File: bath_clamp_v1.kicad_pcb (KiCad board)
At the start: 6 copper layers, 83.8 x 48.3 mm, 163 parts, among them IC1 DAC53401DSGR, J1 105-1103-001, J2 105-1103-001, J3 105-1103-001, J4 HDMI_A, K1 1462042-8, K2 1462042-8, Q1 MBT3904DW1T1G, Q2 BC856, Q3 MBT3904DW1T1G, Q4 MBT3904DW1T1G, U1 OPA828, U10 LP2951-3.3_SOIC, U11 OPA991S, U12 TCA9555DBR, U13 TCA9555DBR, U14 DG412xUE, U15 OPA828, U16 TMUX6111PWR, U17 DG412xUE, U18 AD8421ARZ, U19 TMUX6136PWR, U2 ADG1208, U20 TMUX6111PWR, U21 TMUX6111PWR, U22 TMUX6136PWR, U23 OPA188xxDBV, U24 LMP8350MA_NOPB, U25 OPA2156xD, U3 G6L-1F-TR-DC5, U4 G6L-1F-TR-DC5, U5 G6L-1F-TR-DC5, U6 24AA025UID, U7 LM337L_SO8, U8 OPA2156xD, U9 MCP1804x-3302xOT

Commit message: freerouter updates; close to submission
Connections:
- U20 pad 10: /bath_clamp_v1_1/AMP_OUT -> /bath_clamp_v1_1/INAMP_OUT

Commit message: before autoroute
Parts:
- moved H7 50.1 mm to (4.00, -44.0)
- moved C17 50.0 mm to (13.6, -40.1)
- moved C33 50.0 mm to (37.1, -37.8)
- moved C34 50.0 mm to (31.3, -37.2)
- moved C35 50.0 mm to (34.3, -37.2)
- moved C40 50.0 mm to (77.4, -9.89)
- moved C41 50.0 mm to (44.9, -18.0)
- moved D1 50.0 mm to (70.2, -11.0)
- moved D4 50.0 mm to (68.5, -4.31)
- moved J1 50.0 mm to (79.8, -26.6)
- moved K1 50.0 mm to (70.4, -15.0)
- moved K2 50.0 mm to (70.4, -26.4)
- moved Q3 50.0 mm to (68.8, -7.23)
- moved R11 50.0 mm to (70.0, -7.61)
- moved R12 50.0 mm to (71.7, -7.61)
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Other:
- net class Default: clearance 0.1524 -> 0.127; trace_width 0.1524 -> 0.127; via_dia 0.7 -> 0.6
- rule trace_clearance: 0.1524 -> 0.127

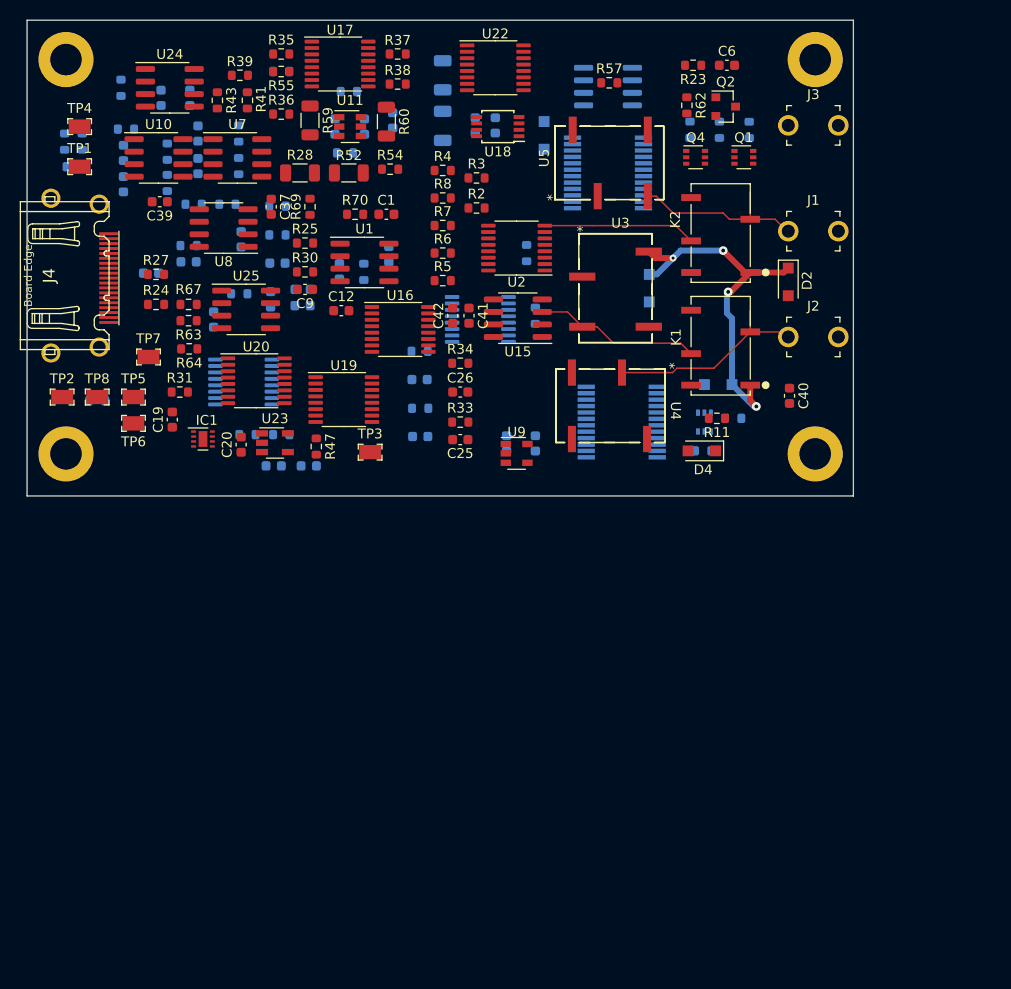
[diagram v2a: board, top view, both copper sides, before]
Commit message: clamp files at submission to JLCPCB
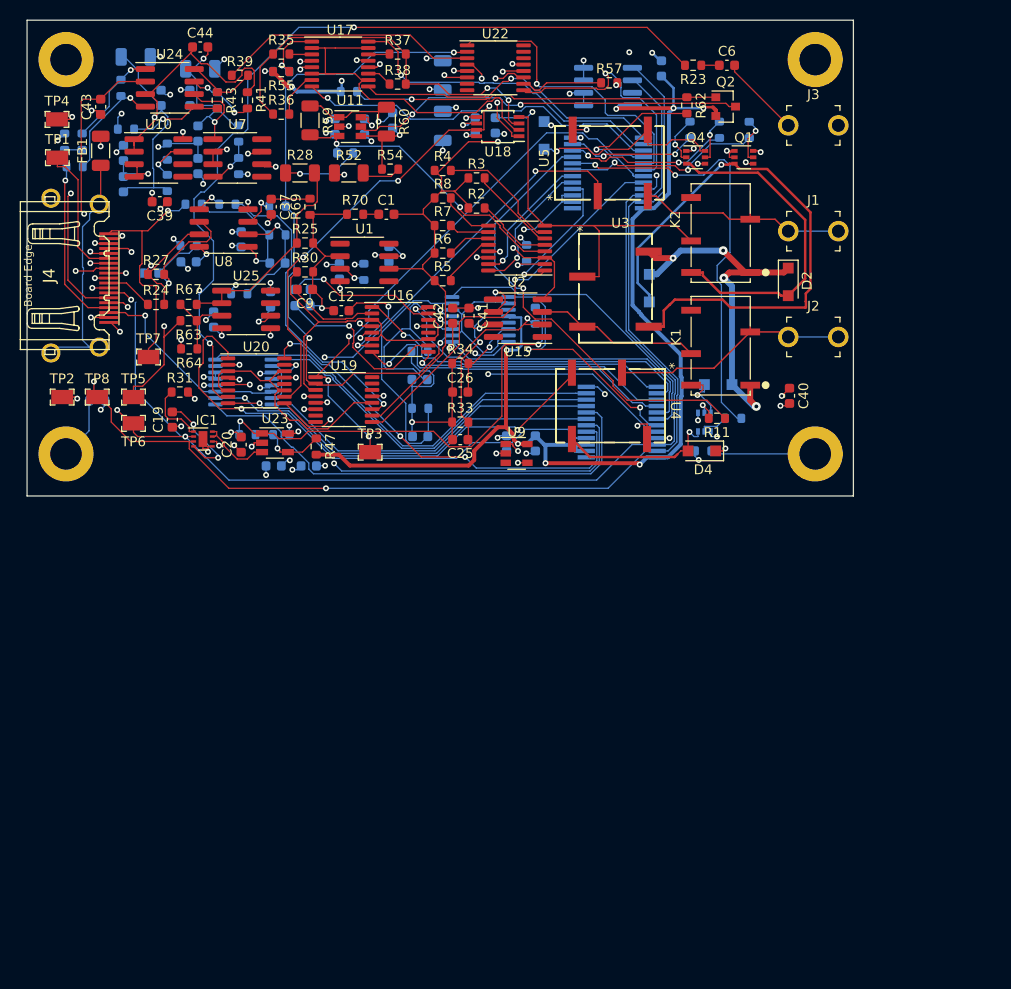
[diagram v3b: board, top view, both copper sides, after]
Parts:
- added C43: 0.1u, Capacitor_SMD:C_0603_1608Metric, F.Cu at (7.52, -39.2)
- added C44: 0.1u, Capacitor_SMD:C_0603_1608Metric, F.Cu at (17.6, -45.3)
- added C45: 10u, Capacitor_SMD:C_1206_3216Metric, B.Cu at (11.1, -44.3)
- added C46: 10u, Capacitor_SMD:C_1206_3216Metric, B.Cu at (17.6, -43.1)
- added C47: 0.1u, Capacitor_SMD:C_0603_1608Metric, B.Cu at (64.4, -43.1)
- added FB1: Ferrite_Bead, Capacitor_SMD:C_1206_3216Metric, F.Cu at (7.52, -34.7)
- added R65: DNI, Resistor_SMD:R_0603_1608Metric, B.Cu at (19.4, -39.9)
- C17, C18: value 0.1u -> 0.01u
- R41: value 1k -> 10k
- moved TP1 2.44 mm to (3.12, -34.0)
- moved TP4 2.41 mm to (3.09, -37.9)
- moved H5 1.22 mm to (4.00, -4.00)
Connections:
- J4 pad SH: GND -> Net-(FB1-Pad1)
- R41 pad 1: +7V -> /bath_clamp_v1_1/adc_driver/LMP_EN
- R41 pad 2: Net-(R41-Pad2) -> +7V
- U24 pad 7: Net-(R41-Pad2) -> /bath_clamp_v1_1/adc_driver/LMP_EN
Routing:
- net +3V3: track 0.00 -> 167.3 mm, vias 0 -> 10
- net /SCL: track 0.00 -> 140.8 mm, vias 0 -> 3
- net /SDA: track 0.00 -> 129.3 mm, vias 0 -> 3
- net GND: track 0.00 -> 121.6 mm, vias 0 -> 77
- net /bath_clamp_v1_1/CC: track 0.00 -> 96.8 mm, vias 0 -> 4
- net /bath_clamp_v1_1/P1_BUF: track 0.00 -> 89.2 mm, vias 0 -> 4
- net /bath_clamp_v1_1/RF_1: track 0.00 -> 60.3 mm, vias 0 -> 2
- net Net-(D3-Pad2): track 0.00 -> 57.3 mm, vias 0 -> 1
- net /bath_clamp_v1_1/FDBK: track 0.00 -> 56.1 mm, vias 0 -> 3
- net /bath_clamp_v1_1/ADC_SEL1: track 0.00 -> 52.9 mm, vias 0 -> 1
- net /bath_clamp_v1_1/CAL_SIG1: track 0.00 -> 49.8 mm, vias 0 -> 3
- net /bath_clamp_v1_1/DAC_SEL1: track 0.00 -> 49.6 mm
- net /bath_clamp_v1_1/CAL_SIG2: track 0.00 -> 48.5 mm, vias 0 -> 3
- net /bath_clamp_v1_1/INAMP_OUT: track 0.00 -> 48.3 mm, vias 0 -> 4
- net +7V: track 0.00 -> 47.7 mm, vias 0 -> 1
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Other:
- net class Power: clearance 0.1778 -> 0.1; trace_width 0.3048 -> 0.127; via_dia 0.889 -> 0.6; via_drill 0.381 -> 0.3
- net class cap_sensitive: clearance 0.3048 -> 0.1; trace_width 0.1524 -> 0.127; via_dia 0.7 -> 0.6
